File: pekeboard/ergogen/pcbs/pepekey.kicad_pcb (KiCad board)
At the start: 2 copper layers, 161.8 x 135.1 mm, 63 parts

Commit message: pekeboard cases
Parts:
- moved PWR1 4.55 mm to (237.9, 75.7)
- moved JST1 0.52 mm to (232.3, 80.7)
- moved RST1 0.36 mm to (237.9, 58.6)
- moved MCU1 0.24 mm to (225.8, 58.6)
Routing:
- net P115: track 169.0 -> 201.0 mm, vias 8 -> 6
- net P100: track 201.0 -> 179.9 mm
- net P113: track 158.0 -> 145.1 mm, vias 1 -> 3
- net P031: track 204.6 -> 217.0 mm, vias 3 -> 7
- net P008: track 193.2 -> 204.0 mm
- net P025: track 122.2 -> 127.3 mm
- net RAW: track 35.4 -> 32.2 mm
- net P002: track 174.6 -> 171.9 mm
- net P106: track 161.5 -> 158.7 mm
- net P011: track 174.1 -> 176.7 mm
- net P022: track 172.7 -> 175.2 mm
- net BAT_P: track 4.55 -> 6.39 mm
- net P024: track 150.8 -> 151.8 mm
- net outer_bottom: track 12.9 -> 12.3 mm
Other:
- outline, holes or cut-outs redrawn

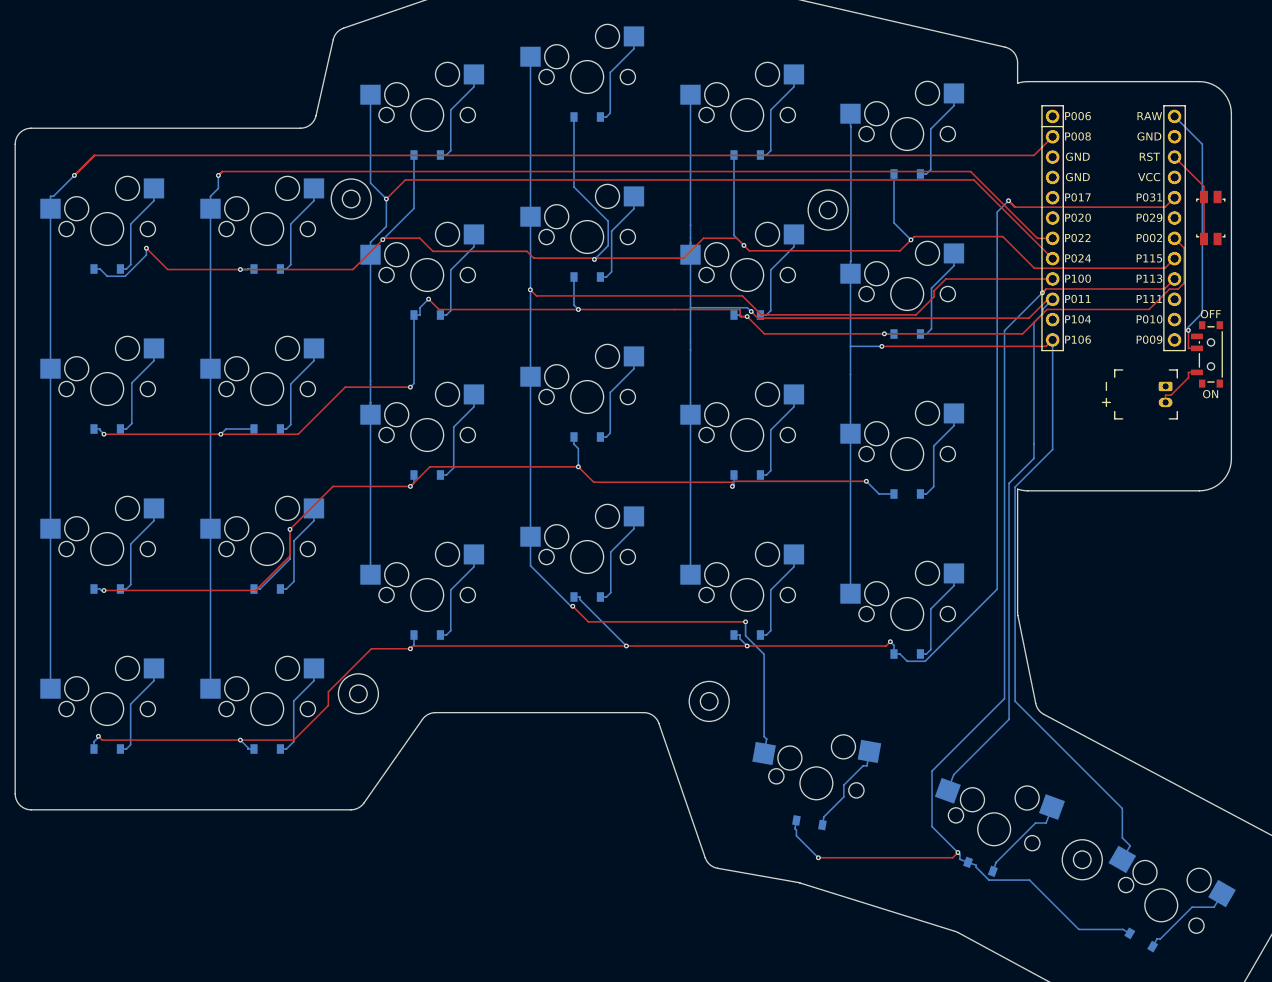
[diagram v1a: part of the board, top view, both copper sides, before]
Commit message: pekeboard case refinement and cutouts
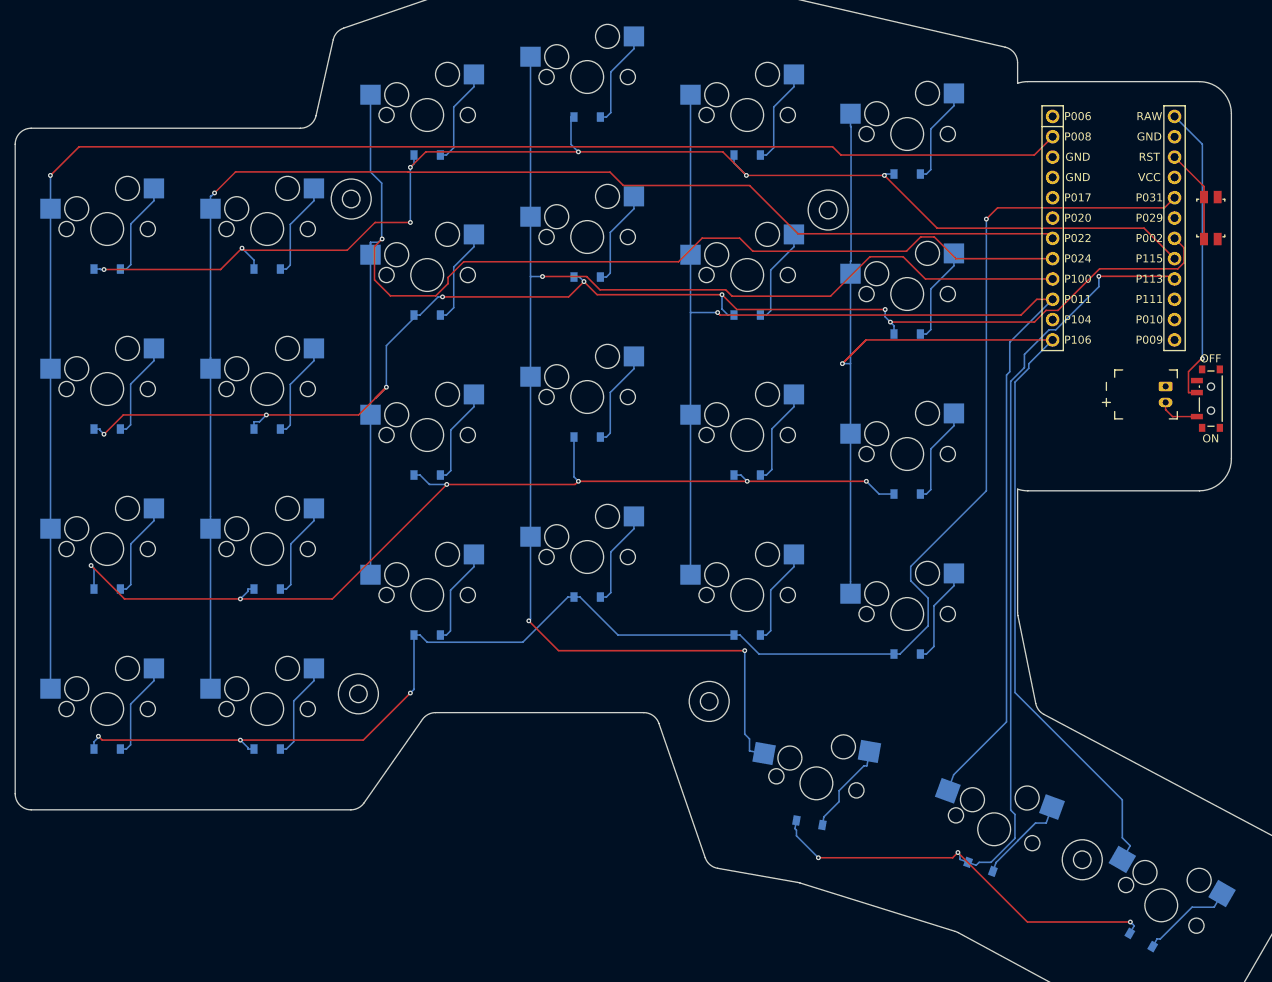
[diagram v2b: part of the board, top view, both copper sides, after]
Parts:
- moved PWR1 5.53 mm to (237.9, 81.2)
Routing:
- net P115: track 201.0 -> 165.5 mm, vias 6 -> 7
- net P106: track 158.7 -> 178.6 mm
- net P031: track 217.0 -> 204.8 mm, vias 7 -> 4
- net P008: track 204.0 -> 192.3 mm
- net P024: track 151.8 -> 160.4 mm
- net RAW: track 32.2 -> 37.8 mm
- net P100: track 179.9 -> 183.3 mm
- net P011: track 176.7 -> 173.4 mm
- net P002: track 171.9 -> 174.5 mm, vias 7 -> 8
- net P022: track 175.2 -> 172.9 mm
- net BAT_P: track 6.39 -> 5.18 mm
- net P025: track 127.3 -> 126.6 mm
- net P113: track 145.1 -> 145.0 mm, vias 3 -> 4

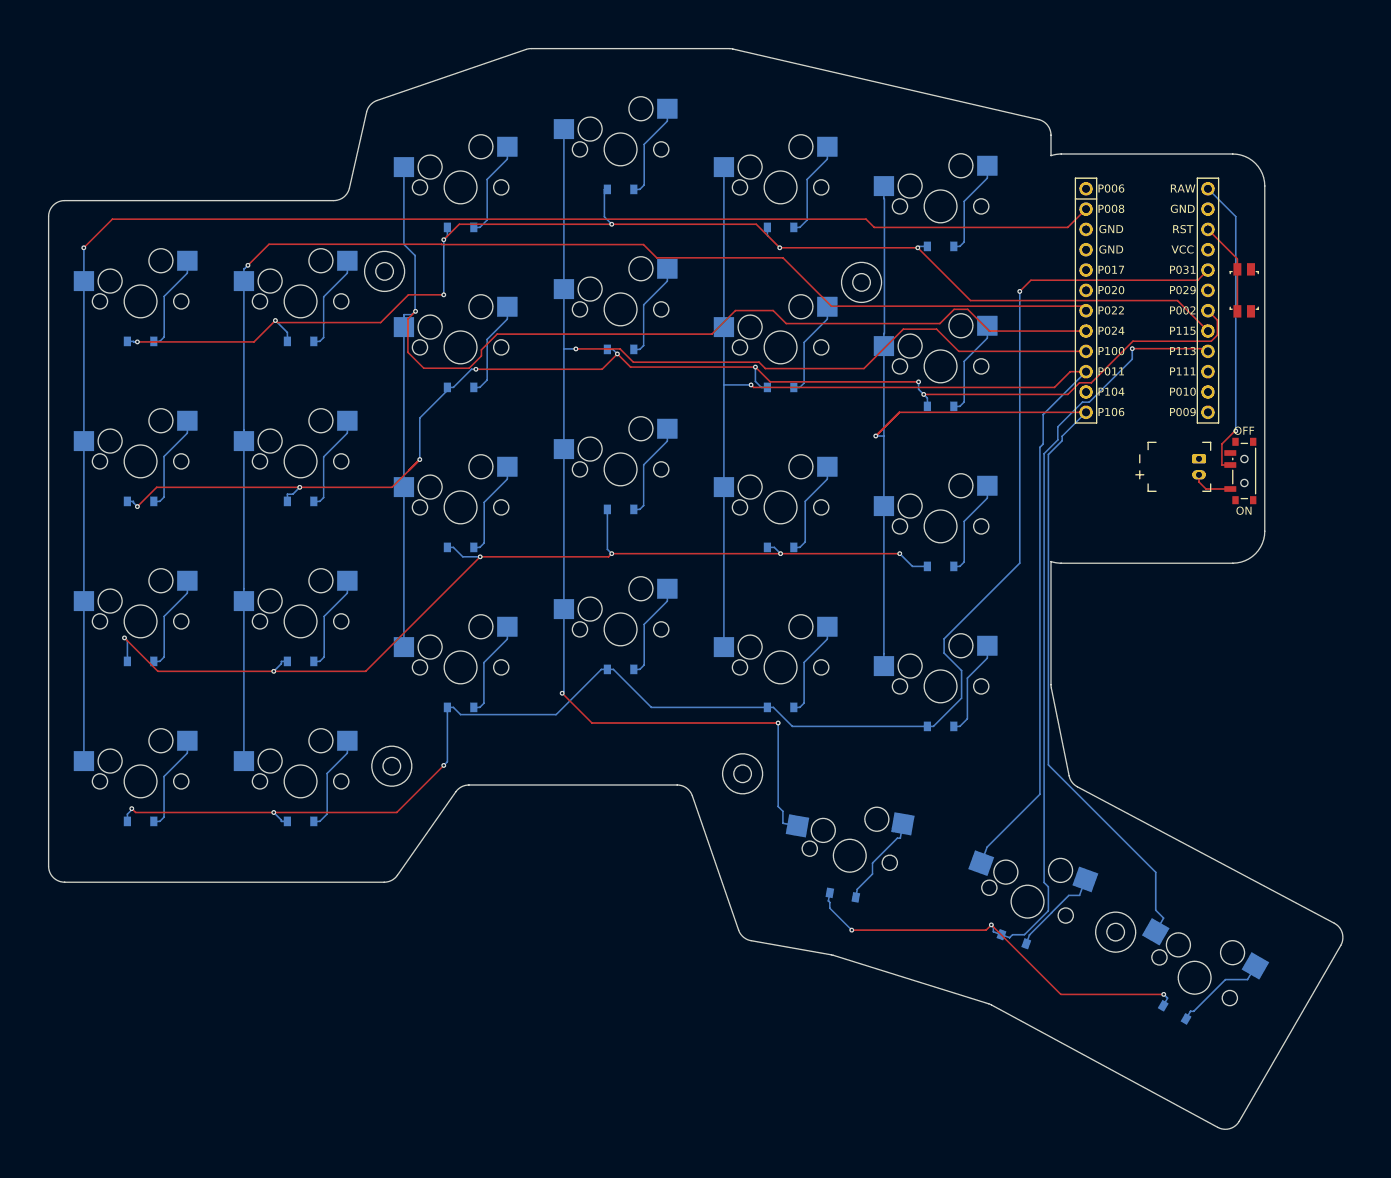
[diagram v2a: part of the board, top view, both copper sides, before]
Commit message: Battery area and cover
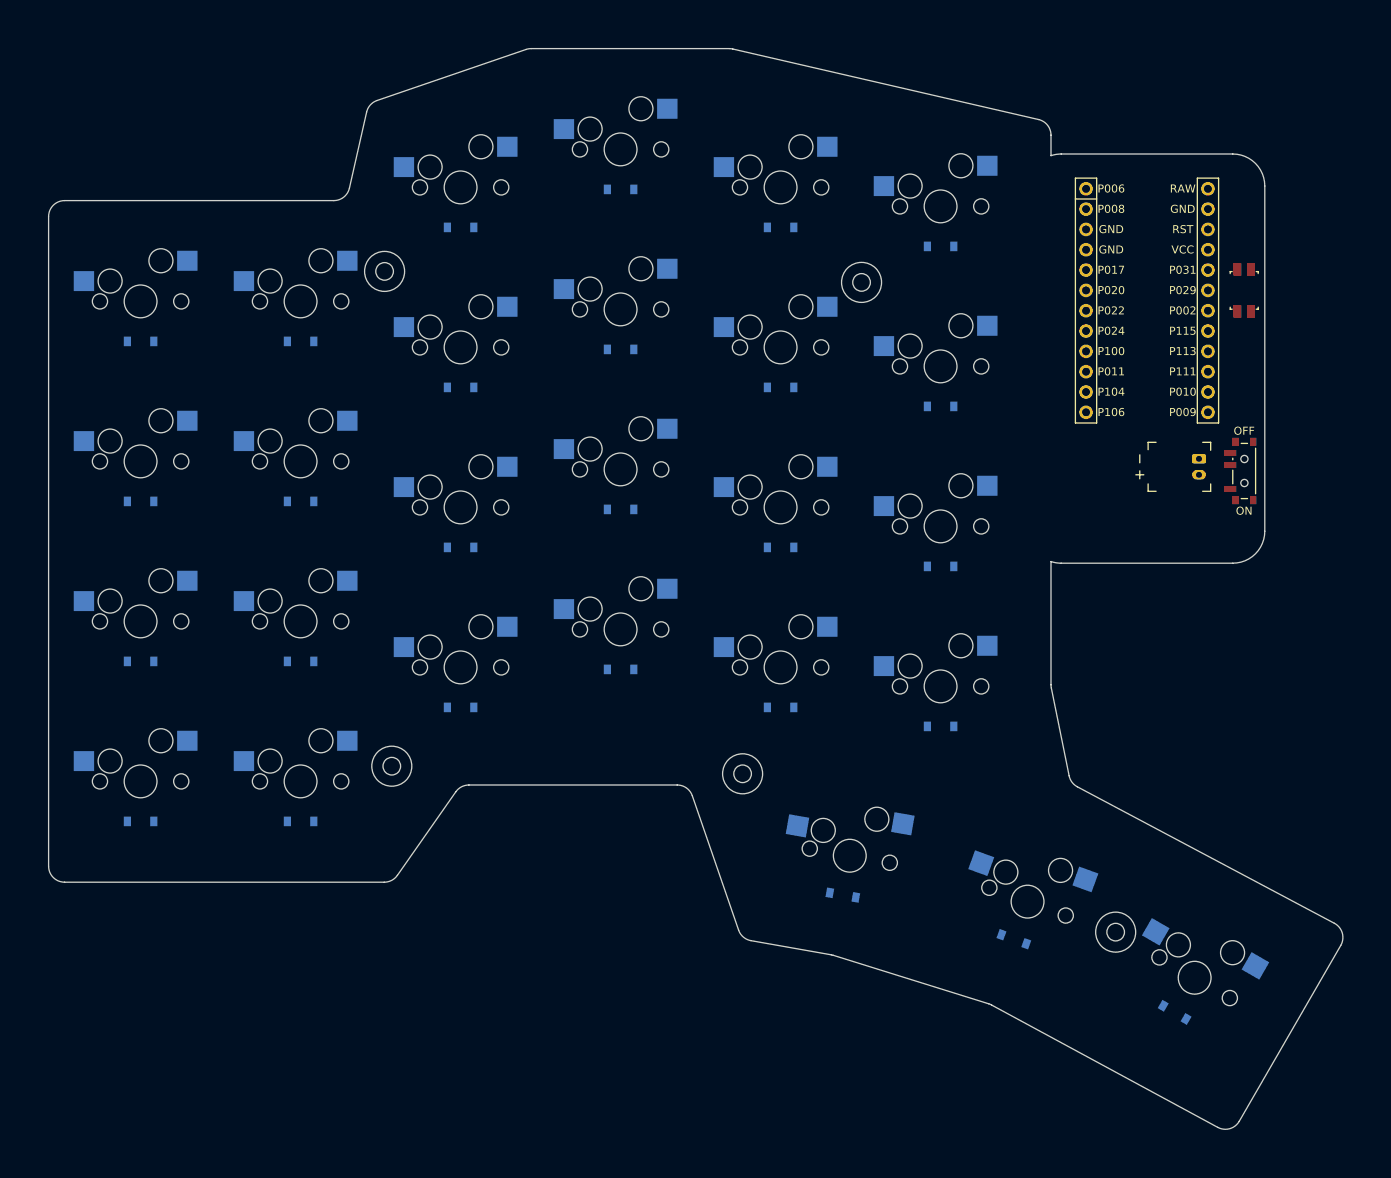
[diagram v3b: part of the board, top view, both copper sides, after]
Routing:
- net P031: track 204.8 -> 0.00 mm, vias 4 -> 0
- net P008: track 192.3 -> 0.00 mm, vias 1 -> 0
- net P100: track 183.3 -> 0.00 mm, vias 3 -> 0
- net P106: track 178.6 -> 0.00 mm, vias 1 -> 0
- net P002: track 174.5 -> 0.00 mm, vias 8 -> 0
- net P011: track 173.4 -> 0.00 mm, vias 1 -> 0
- net P022: track 172.9 -> 0.00 mm, vias 1 -> 0
- net P115: track 165.5 -> 0.00 mm, vias 7 -> 0
- net P024: track 160.4 -> 0.00 mm, vias 1 -> 0
- net P113: track 145.0 -> 0.00 mm, vias 4 -> 0
- net P025: track 126.6 -> 0.00 mm, vias 6 -> 0
- net RAW: track 37.8 -> 0.00 mm, vias 1 -> 0
- net ring_bottom: track 12.3 -> 0.00 mm
- net middle_num: track 12.3 -> 0.00 mm
- net ring_home: track 12.3 -> 0.00 mm
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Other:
- outline, holes or cut-outs redrawn

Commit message: Fixing keys spacing More case and battery space refinements
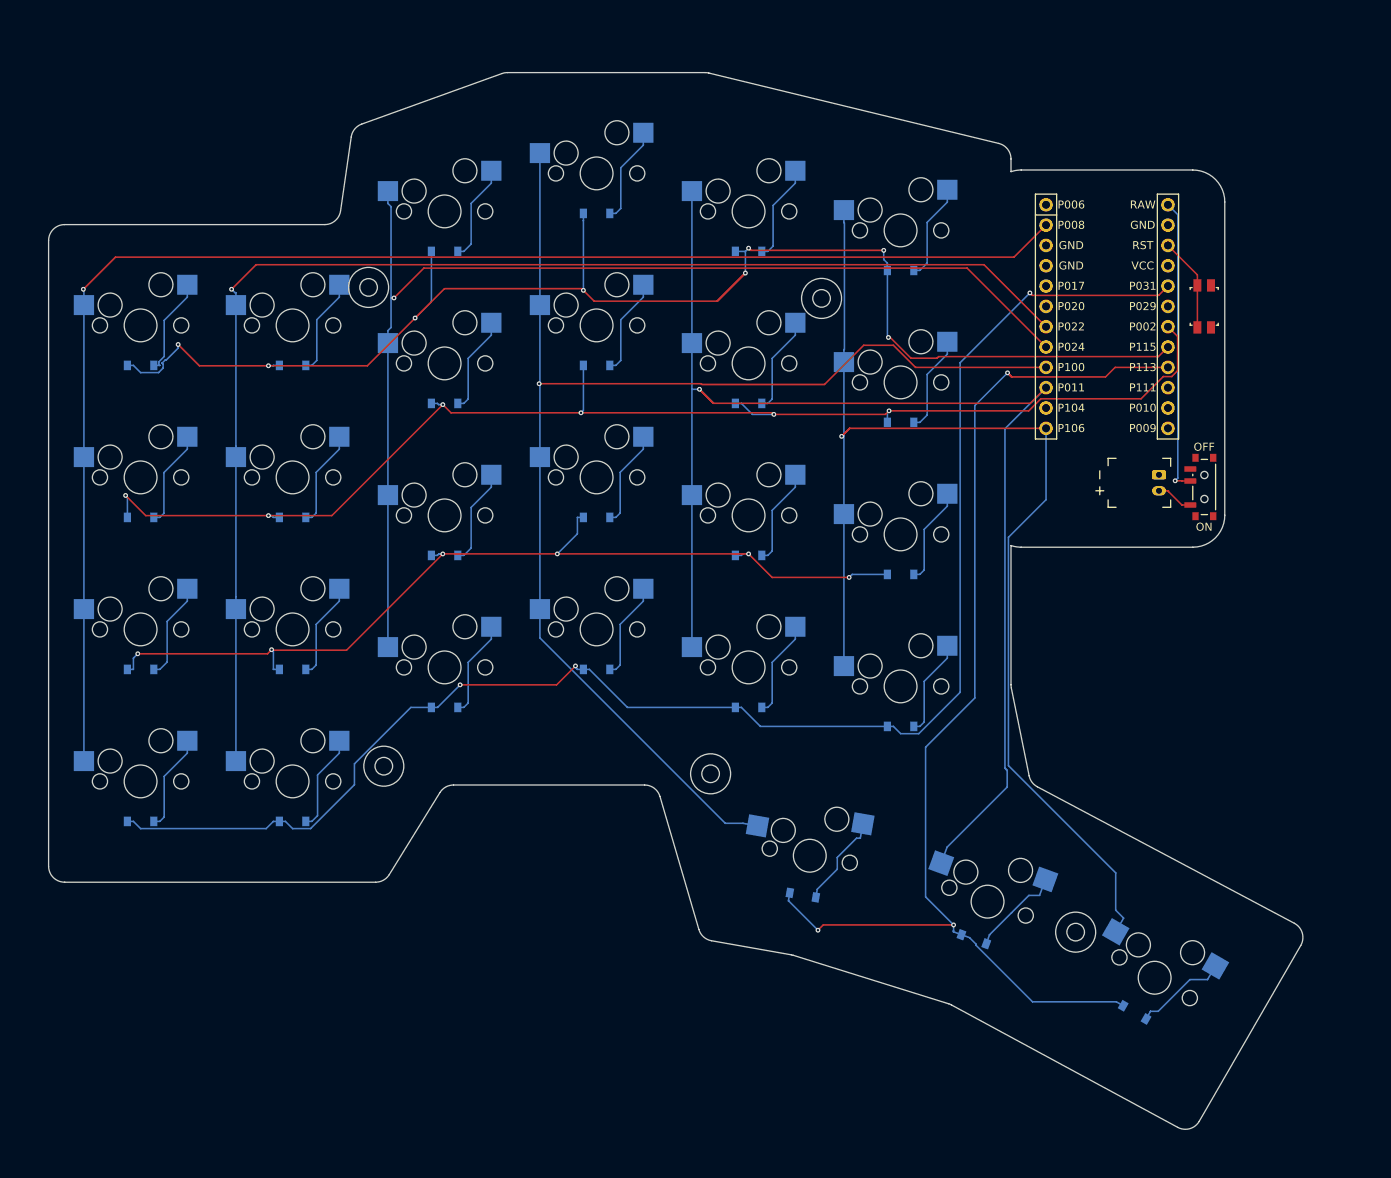
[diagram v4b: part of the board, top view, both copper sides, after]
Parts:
- moved D24 5.83 mm to (195.0, 56.1)
- moved S24 5.83 mm to (195.0, 51.1)
- moved PWR1 5.39 mm to (232.9, 83.2)
- moved RST1 5.39 mm to (232.9, 60.6)
- moved D23 5.39 mm to (195.0, 75.1)
- moved JST1 5.39 mm to (227.3, 82.7)
- moved MCU1 5.39 mm to (220.8, 60.6)
- moved MH3 5.39 mm to (185.1, 59.6)
- moved S23 5.39 mm to (195.0, 70.1)
- moved D22 5.10 mm to (195.0, 94.1)
- moved S22 5.10 mm to (195.0, 89.1)
- moved D25 5.00 mm to (182.8, 134.2)
- moved MH5 5.00 mm to (216.9, 138.8)
- moved D20 5.00 mm to (176.0, 53.8)
- moved D21 5.00 mm to (195.0, 113.1)
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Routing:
- net P115: track 0.00 -> 197.9 mm, vias 0 -> 8
- net P031: track 0.00 -> 192.3 mm, vias 0 -> 3
- net P008: track 0.00 -> 182.7 mm, vias 0 -> 1
- net P011: track 0.00 -> 177.8 mm, vias 0 -> 1
- net P022: track 0.00 -> 166.9 mm, vias 0 -> 1
- net P002: track 0.00 -> 165.8 mm, vias 0 -> 6
- net P100: track 0.00 -> 164.1 mm, vias 0 -> 1
- net P106: track 0.00 -> 160.1 mm, vias 0 -> 1
- net P113: track 0.00 -> 147.6 mm, vias 0 -> 3
- net P024: track 0.00 -> 144.8 mm, vias 0 -> 1
- net P025: track 0.00 -> 116.1 mm, vias 0 -> 6
- net RAW: track 0.00 -> 37.1 mm, vias 0 -> 1
- net outer_num: track 0.00 -> 12.4 mm
- net middle_num: track 0.00 -> 12.3 mm
- net inner_home: track 0.00 -> 12.3 mm
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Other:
- board size 161.8 x 135.1 mm -> 156.8 x 132.1 mm

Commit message: Extreme trimming
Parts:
- moved MH4 14.1 mm to (166.5, 105.8)
- moved MH2 7.83 mm to (128.5, 110.5)
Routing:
- net P115: track 197.9 -> 0.00 mm, vias 8 -> 0
- net P031: track 192.3 -> 0.00 mm, vias 3 -> 0
- net P008: track 182.7 -> 0.00 mm, vias 1 -> 0
- net P011: track 177.8 -> 0.00 mm, vias 1 -> 0
- net P022: track 166.9 -> 0.00 mm, vias 1 -> 0
- net P002: track 165.8 -> 0.00 mm, vias 6 -> 0
- net P100: track 164.1 -> 0.00 mm, vias 1 -> 0
- net P106: track 160.1 -> 0.00 mm, vias 1 -> 0
- net P113: track 147.6 -> 0.00 mm, vias 3 -> 0
- net P024: track 144.8 -> 0.00 mm, vias 1 -> 0
- net P025: track 116.1 -> 0.00 mm, vias 6 -> 0
- net RAW: track 37.1 -> 0.00 mm, vias 1 -> 0
- net outer_num: track 12.4 -> 0.00 mm
- net middle_num: track 12.3 -> 0.00 mm
- net inner_home: track 12.3 -> 0.00 mm
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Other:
- board size 156.8 x 132.1 mm -> 150.9 x 124.7 mm
